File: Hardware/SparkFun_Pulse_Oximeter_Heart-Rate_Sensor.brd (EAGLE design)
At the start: 25.4 x 12.7 mm, 53 parts, among them U1 MAX30101EFD, U2 MAX32664GWEA, U3 1.8V/100mA, Y1 32.768kHz

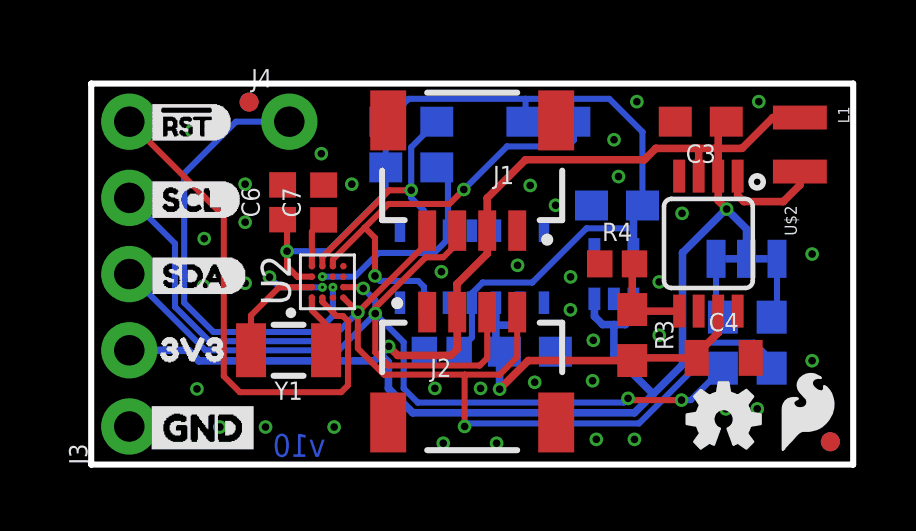
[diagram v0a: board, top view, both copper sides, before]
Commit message: Updates silk, updates bio sensor hub to slightly improved package, rolls version to v11
* Updates schematic to include part numbers on all parts
* Updates notes on parts
* Updates package size on 0402 components to 0402-tight
* Adds more vias
* Adds more measures
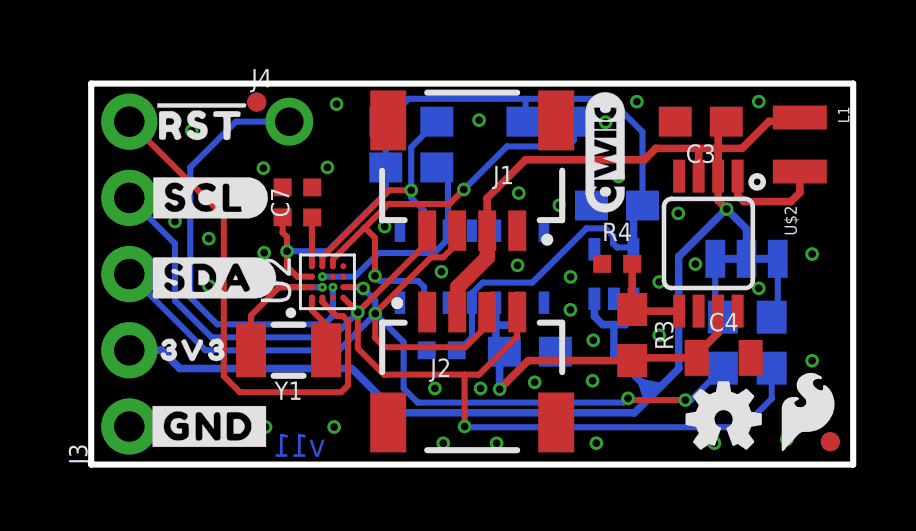
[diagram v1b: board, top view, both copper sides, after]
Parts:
- removed U$14: (no value), oximeter:OXIMETER0
- removed U$15: (no value), Heart Rate:HEART_RATE0
- removed U$16: (no value), Monitor:MONITOR0
- removed U$18: (no value), and:AND0
- removed U$19: (no value), SparkFun-Aesthetics:SFE_LOGO_FLAME_.1
- added LOGO5: QWIIC_LOGO_4MM, SparkFun-Aesthetics:QWIIC_4MM
- added U$21: (no value), bot:HEART_RATE_MONITOR37
- C2, C6, C7: device SparkFun-Capacitors:0402 -> SparkFun-Capacitors:0402-TIGHT
- J1, J2: value (none) -> QWIIC_RIGHT_ANGLE
- R4: value 100K -> 100k; device SparkFun-Resistors:0402 -> SparkFun-Resistors:0402-TIGHT
- U$1: device Labels:I_SUPER2_C-()-03 -> topmirror:#I2C#1348
- U$10: device SDA:SDA0 -> top:#SDA#9
- U$11: device Labels:GND-03 -> bot:#SCL#9
- U$12: device Labels:3V3-03 -> topmirror:#RST#32
- U$13: device Labels:3V3-TEXT -> bot:##MFIO##12
- U$17: device Pulse:PULSE0 -> bot:PULSE35
- U$20: device SDA_TOP:SDA0 -> bot:OXIMETER_AND36
- U$3, U$5: device Labels:GND-03 -> top:#GND#0
- U$4: device buzzard_labels:SCL0 -> topmirror:#SCL#7
- U$6: device RST_BAR:#RST0 -> topmirror:#RST#32
- U$7: device MFIO:MFIO0 -> bot:3V338
- U$8: device RST_BOT:#RST0 -> botmirror:#SDA#10
- U$9: device SCL:SCL0 -> top:#3V3#1
- moved LOGO4 88.9 mm to (38.6, 50.8)
- moved U$20 20.1 mm to (21.2, 10.9), flipped to the bottom
- moved U$11 7.94 mm to (3.81, 8.89), turned to 0 degrees
- moved U$7 7.92 mm to (3.43, 3.81), flipped to the top, turned to 0 degrees
- moved U$12 7.90 mm to (3.68, 11.4)
- moved U$13 7.02 mm to (6.73, 8.64), flipped to the bottom, turned to 270 degrees
- moved U$8 5.23 mm to (3.94, 6.22), flipped to the top
- moved U$9 5.13 mm to (3.94, 3.81)
- moved U$1 2.67 mm to (21.7, 8.51), turned to 0 degrees
- moved U$5 2.34 mm to (3.94, 1.27), flipped to the bottom
- moved U$17 2.29 mm to (23.4, 11.9)
- moved U$4 2.13 mm to (3.81, 8.89)
- moved U$6 2.13 mm to (3.68, 11.4)
- moved U$3 1.94 mm to (3.94, 1.27), flipped to the top
- moved U$10 1.50 mm to (3.68, 6.22)
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- renumbered JP1 to I2C
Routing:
- net 3.3V: track 57.9 -> 54.3 mm, vias 2 -> 1
- net HOST_SDA: track 36.8 -> 35.2 mm
- net HOST_SCL: track 38.1 -> 37.0 mm
- net !MFIO: track 15.1 -> 14.5 mm
- net 1.8V: track 31.6 -> 32.2 mm
- net GND: vias 40 -> 42
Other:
- board text added: "v11"
- board text removed: "v10"

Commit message: Adds new panel
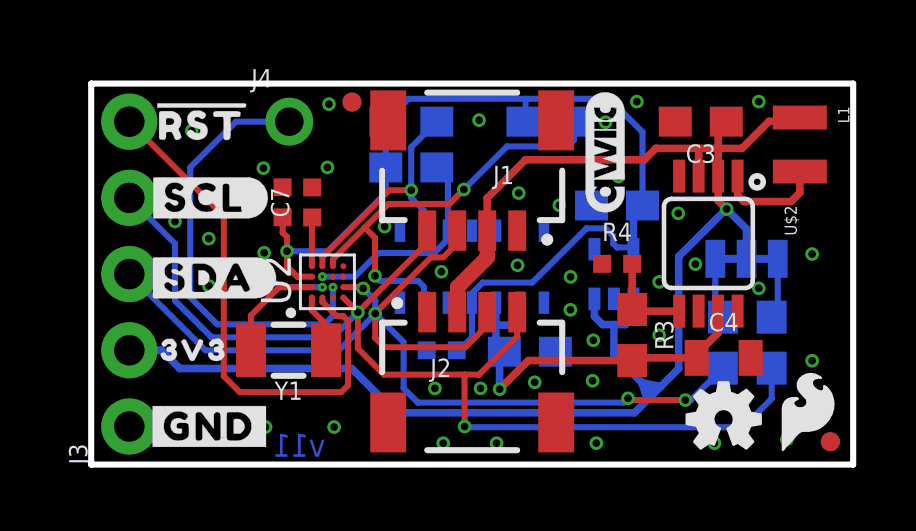
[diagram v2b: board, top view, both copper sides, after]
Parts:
- moved FD1 3.18 mm to (8.69, 12.1)
- moved FD2 3.17 mm to (8.69, 12.1)
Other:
- board text added: "2-Layer Board"
- board text added: "Finish: Lead-Free HASL"
- board text added: "Soldermask: Red Silk: White"
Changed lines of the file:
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@@
 <drawing>
 <settings>
-<setting alwaysvectorfont="yes"/>
+<setting alwaysvectorfont="no"/>
 <setting verticaltext="up"/>
 </settings>
-<grid distance="0.05" unitdist="inch" unit="inch" style="dots" multiple="1" display="yes" altdistance="0.001" altunitdist="inch" altunit="inch"/>
+<grid distance="0.05" unitdist="inch" unit="inch" style="dots" multiple="1" display="yes" altdistance="0.005" altunitdist="inch" altunit="inch"/>
 <layers>
 <layer number="1" name="Top" color="4" fill="1" visible="yes" active="yes"/>
@@
 <layer number="23" name="tOrigins" color="15" fill="1" visible="yes" active="yes"/>
 <layer number="24" name="bOrigins" color="15" fill="1" visible="yes" active="yes"/>
-<layer number="25" name="tNames" color="7" fill="1" visible="no" active="yes"/>
-<layer number="26" name="bNames" color="7" fill="1" visible="no" active="yes"/>
-<layer number="27" name="tValues" color="7" fill="1" visible="no" active="yes"/>
-<layer number="28" name="bValues" color="7" fill="1" visible="no" active="yes"/>
-<layer number="29" name="tStop" color="7" fill="3" visible="no" active="yes"/>
-<layer number="30" name="bStop" color="7" fill="6" visible="no" active="yes"/>
-<layer number="31" name="tCream" color="7" fill="4" visible="no" active="yes"/>
-<layer number="32" name="bCream" color="7" fill="5" visible="no" active="yes"/>
-<layer number="33" name="tFinish" color="6" fill="3" visible="no" active="yes"/>
-<layer number="34" name="bFinish" color="6" fill="6" visible="no" active="yes"/>
-<layer number="35" name="tGlue" color="7" fill="4" visible="no" active="yes"/>
-<layer number="36" name="bGlue" color="7" fill="5" visible="no" active="yes"/>
-<layer number="37" name="tTest" color="7" fill="1" visible="no" active="yes"/>
-<layer number="38" name="bTest" color="7" fill="1" visible="no" active="yes"/>
-<layer number="39" name="tKeepout" color="4" fill="11" visible="no" active="yes"/>
-<layer number="40" name="bKeepout" color="1" fill="11" visible="no" active="yes"/>
-<layer number="41" name="tRestrict" color="4" fill="10" visible="no" active="yes"/>
-<layer number="42" name="bRestrict" color="1" fill="10" visible="no" active="yes"/>
-<layer number="43" name="vRestrict" color="2" fill="10" visible="no" active="yes"/>
-<layer number="44" name="Drills" color="7" fill="1" visible="no" active="yes"/>
+<layer number="25" name="tNames" color="7" fill="1" visible="yes" active="yes"/>
+<layer number="26" name="bNames" color="7" fill="1" visible="yes" active="yes"/>
+<layer number="27" name="tValues" color="7" fill="1" visible="yes" active="yes"/>
+<layer number="28" name="bValues" color="7" fill="1" visible="yes" active="yes"/>
+<layer number="29" name="tStop" color="7" fill="3" visible="yes" active="yes"/>
+<layer number="30" name="bStop" color="7" fill="6" visible="yes" active="yes"/>
+<layer number="31" name="tCream" color="7" fill="4" visible="yes" active="yes"/>
+<layer number="32" name="bCream" color="7" fill="5" visible="yes" active="yes"/>
+<layer number="33" name="tFinish" color="6" fill="3" visible="yes" active="yes"/>
+<layer number="34" name="bFinish" color="6" fill="6" visible="yes" active="yes"/>
+<layer number="35" name="tGlue" color="7" fill="4" visible="yes" active="yes"/>
+<layer number="36" name="bGlue" color="7" fill="5" visible="yes" active="yes"/>
+<layer number="37" name="tTest" color="7" fill="1" visible="yes" active="yes"/>
+<layer number="38" name="bTest" color="7" fill="1" visible="yes" active="yes"/>
+<layer number="39" name="tKeepout" color="4" fill="11" visible="yes" active="yes"/>
+<layer number="40" name="bKeepout" color="1" fill="11" visible="yes" active="yes"/>
+<layer number="41" name="tRestrict" color="4" fill="10" visible="yes" active="yes"/>
+<layer number="42" name="bRestrict" color="1" fill="10" visible="yes" active="yes"/>
+<layer number="43" name="vRestrict" color="2" fill="10" visible="yes" active="yes"/>
+<layer number="44" name="Drills" color="7" fill="1" visible="yes" active="yes"/>
 <layer number="45" name="Holes" color="7" fill="1" visible="yes" active="yes"/>
-<layer number="46" name="Milling" color="3" fill="1" visible="no" active="yes"/>
+<layer number="46" name="Milling" color="3" fill="1" visible="yes" active="yes"/>
 <layer number="47" name="Measures" color="7" fill="1" visible="yes" active="yes"/>
-<layer number="48" name="Document" color="7" fill="1" visible="no" active="yes"/>
+<layer number="48" name="Document" color="7" fill="1" visible="yes" active="yes"/>
 <layer number="49" name="Reference" color="13" fill="1" visible="yes" active="yes"/>
 <layer number="50" name="dxf" color="7" fill="1" visible="no" active="no"/>
 <layer number="51" name="tDocu" color="6" fill="1" visible="yes" active="yes"/>
-<layer number="52" name="bDocu" color="7" fill="1" visible="no" active="yes"/>
+<layer number="52" name="bDocu" color="7" fill="1" visible="yes" active="yes"/>
 <layer number="53" name="tGND_GNDA" color="7" fill="9" visible="no" active="no"/>
 <layer number="54" name="bGND_GNDA" color="1" fill="9" visible="no" active="no"/>
@@
 <layer number="115" name="ReferenceISLANDS" color="7" fill="1" visible="no" active="no"/>
 <layer number="116" name="Patch_BOT" color="9" fill="4" visible="no" active="no"/>
-<layer number="117" name="PM_Ref" color="26" fill="1" visible="no" active="yes"/>
+<layer number="117" name="PM_Ref" color="26" fill="1" visible="yes" active="yes"/>
 <layer number="118" name="Rect_Pads" color="7" fill="1" visible="no" active="no"/>
-<layer number="119" name="PF_Ref" color="31" fill="1" visible="no" active="yes"/>
-<layer number="120" name="WFL_Ref" color="25" fill="1" visible="no" active="yes"/>
+<layer number="119" name="PF_Ref" color="31" fill="1" visible="yes" active="yes"/>
+<layer number="120" name="WFL_Ref" color="25" fill="1" visible="yes" active="yes"/>
 <layer number="121" name="_tsilk" color="7" fill="1" visible="no" active="no"/>
 <layer number="122" name="_bsilk" color="7" fill="1" visible="no" active="no"/>
@@
 <text x="22.352" y="-10.16" size="1.778" layer="51" font="vector">Elias Santistevan</text>
 <text x="7.807959375" y="0.25908125" size="0.762" layer="16" font="vector" ratio="15" rot="MR0">v11</text>
-<text x="41.402" y="36.83" size="2.032" layer="51" font="vector">Via on Pad for small BGA</text>
+<text x="41.91" y="36.83" size="1.778" layer="51" font="vector" ratio="15">Via on Pad for small BGA</text>
 <dimension x1="25.4" y1="12.7" x2="0" y2="12.7" x3="12.7" y3="18.034" textsize="2.54" textratio="15" layer="47" dtype="horizontal" unit="inch"/>
 <dimension x1="25.4" y1="0" x2="25.4" y2="12.7" x3="32.766" y3="6.35" textsize="2.54" textratio="15" layer="47" dtype="horizontal" unit="inch"/>
@@
 <dimension x1="0" y1="12.7" x2="0" y2="0" x3="-10.16" y3="6.35" textsize="1.778" textratio="15" layer="47" unit="inch"/>
 <dimension x1="12.7" y1="6.604" x2="12.7" y2="0" x3="-6.35" y3="3.302" textsize="1.524" textratio="15" layer="47" unit="inch"/>
+<text x="41.91" y="33.02" size="1.778" layer="51" font="vector" ratio="15">Finish: Lead-Free HASL</text>
+<text x="41.91" y="29.21" size="1.778" layer="51" font="vector" ratio="15">2-Layer Board</text>
+<text x="41.91" y="22.86" size="1.778" layer="51" font="vector" ratio="15">Soldermask: Red
+Silk: White</text>
 </plain>
 <attributes>
@@
 <element name="LOGO2" library="SparkFun-Aesthetics" package="OSHW-LOGO-MINI" value="OSHW-LOGOMINI" x="21.082" y="1.524" smashed="yes"/>
 <element name="LOGO3" library="SparkFun-Aesthetics" package="SFE_LOGO_NAME_.1" value="SFE_LOGO_NAME.1_INCH" x="13.208" y="1.778" smashed="yes" rot="MR0"/>
-<element name="FD1" library="SparkFun-Aesthetics" package="FIDUCIAL-MICRO" value="FIDUCIALUFIDUCIAL" x="5.516878125" y="12.082778125" smashed="yes" rot="MR0"/>
-<element name="FD2" library="SparkFun-Aesthetics" package="FIDUCIAL-MICRO" value="FIDUCIALUFIDUCIAL" x="5.519421875" y="12.082778125" smashed="yes"/>
+<element name="FD1" library="SparkFun-Aesthetics" package="FIDUCIAL-MICRO" value="FIDUCIALUFIDUCIAL" x="8.691878125" y="12.082778125" smashed="yes" rot="MR0"/>
+<element name="FD2" library="SparkFun-Aesthetics" package="FIDUCIAL-MICRO" value="FIDUCIALUFIDUCIAL" x="8.694421875" y="12.082778125" smashed="yes"/>
 <element name="FD3" library="SparkFun-Aesthetics" package="FIDUCIAL-MICRO" value="FIDUCIALUFIDUCIAL" x="24.638" y="0.762" smashed="yes" rot="MR0"/>
 <element name="FD4" library="SparkFun-Aesthetics" package="FIDUCIAL-MICRO" value="FIDUCIALUFIDUCIAL" x="24.638" y="0.762" smashed="yes"/>
@@
 <via x="5.7658" y="7.0612" extent="1-16" drill="0.254"/>
 <via x="23.187665625" y="0.840740625" extent="1-16" drill="0.254"/>
-<via x="8.1788" y="12.0142" extent="1-16" drill="0.254"/>
+<via x="7.9248" y="12.0142" extent="1-16" drill="0.254"/>
 <via x="20.139665625" y="6.682740625" extent="1-16" drill="0.254"/>
 <via x="22.25294375" y="5.87501875" extent="1-16" drill="0.254"/>
@@
 </drawing>
 <compatibility>
+<note version="6.3" minversion="6.2.2" severity="warning">
+Since Version 6.2.2 text objects can contain more than one line,
+which will not be processed correctly with this version.
+</note>
 <note version="8.3" severity="warning">
 Since Version 8.3, EAGLE supports URNs for individual library
